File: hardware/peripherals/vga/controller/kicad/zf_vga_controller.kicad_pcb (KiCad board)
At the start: 2 copper layers, 98 x 40 mm, 17 parts, among them J1 Conn_01x09, Q1 BC547, SW1 SW_Push_Dual, SW2 SW_Push_Dual, SW3 SW_Push_Dual, SW4 SW_Push_Dual, SW5 SW_Push_Dual, SW6 SW_Push_Dual, U1 74HC541

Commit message: Final controller and Gerber files
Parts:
- removed the Mount1 at (234.0, 71.0)
- removed the Mount1 at (234.0, 39.0)
- added Mount1: MountingHole_3.2mm_M3_Pad, MountingHole:MountingHole_3.2mm_M3_Pad, F.Cu at (236.0, 71.0)
- added Mount1: MountingHole_3.2mm_M3_Pad, MountingHole:MountingHole_3.2mm_M3_Pad, F.Cu at (236.0, 39.0)
- moved R1 14.3 mm to (225.0, 38.8)
- moved R2 12.0 mm to (225.0, 42.5), turned to 180 degrees
- moved SW6 11.1 mm to (229.7, 55.0), turned to 45 degrees
- moved Q1 9.53 mm to (217.4, 46.4)
- moved SW5 9.40 mm to (220.0, 64.7), turned to 315 degrees
- moved SW1 0.05 mm to (160.0, 45.3)
- moved SW2 0.05 mm to (160.0, 64.7)
- moved SW3 0.05 mm to (150.3, 55.0)
- moved SW4 0.05 mm to (169.7, 55.0)
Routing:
- net Net-(RN1-Pad7): track 54.0 -> 34.1 mm
- net Net-(RN1-Pad6): track 15.6 -> 30.1 mm
- net Net-(SW5-Pad2): track 21.4 -> 33.3 mm
- net Net-(SW6-Pad2): track 22.7 -> 34.4 mm
- net Net-(Q1-Pad2): track 6.05 -> 13.3 mm
- net Net-(Q1-Pad1): track 40.8 -> 35.1 mm
- net Net-(J1-Pad9): track 11.5 -> 7.98 mm
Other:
- board size 98 x 40 mm -> 100 x 40 mm
- board text added: "Z-FIGHTER VGA Controller @tangent3D 2022"
- board text removed: "Z-FIGHTER VGA Module Controller @tangent3D 2022"

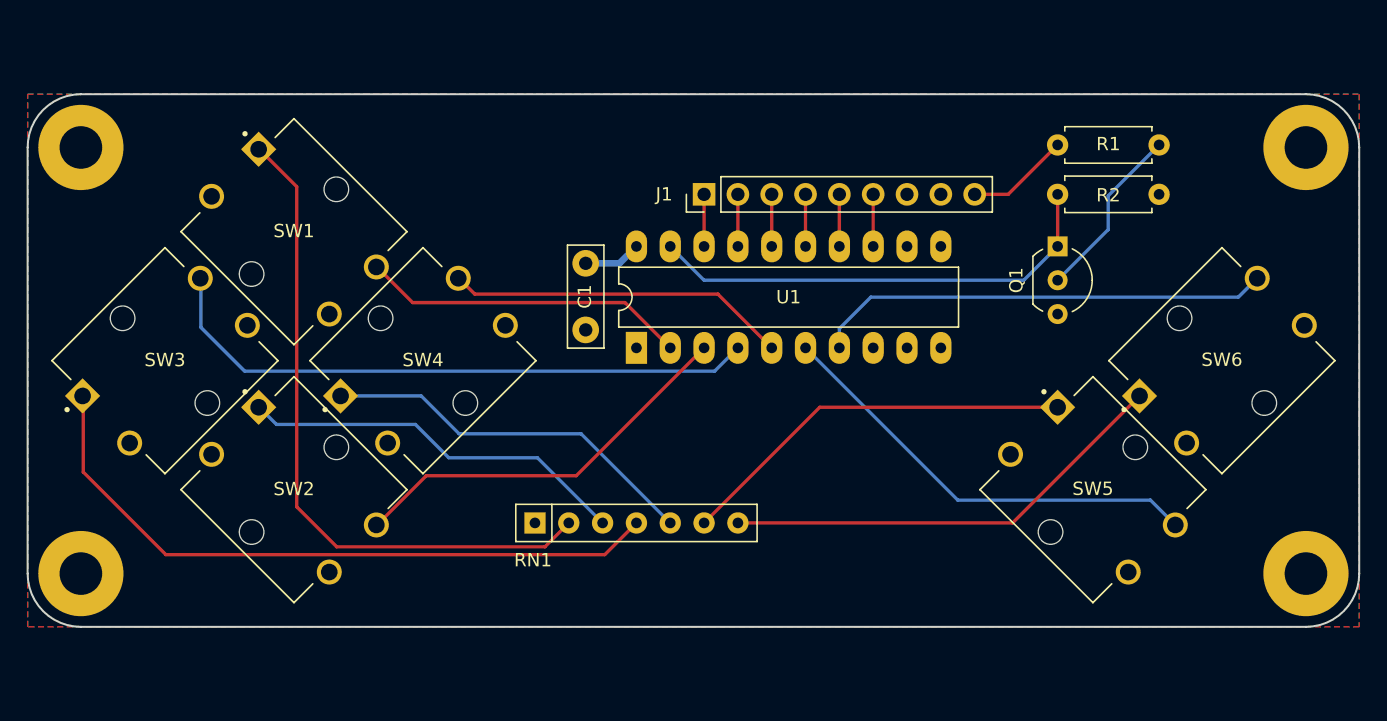
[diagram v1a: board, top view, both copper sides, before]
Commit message: Rounded corners
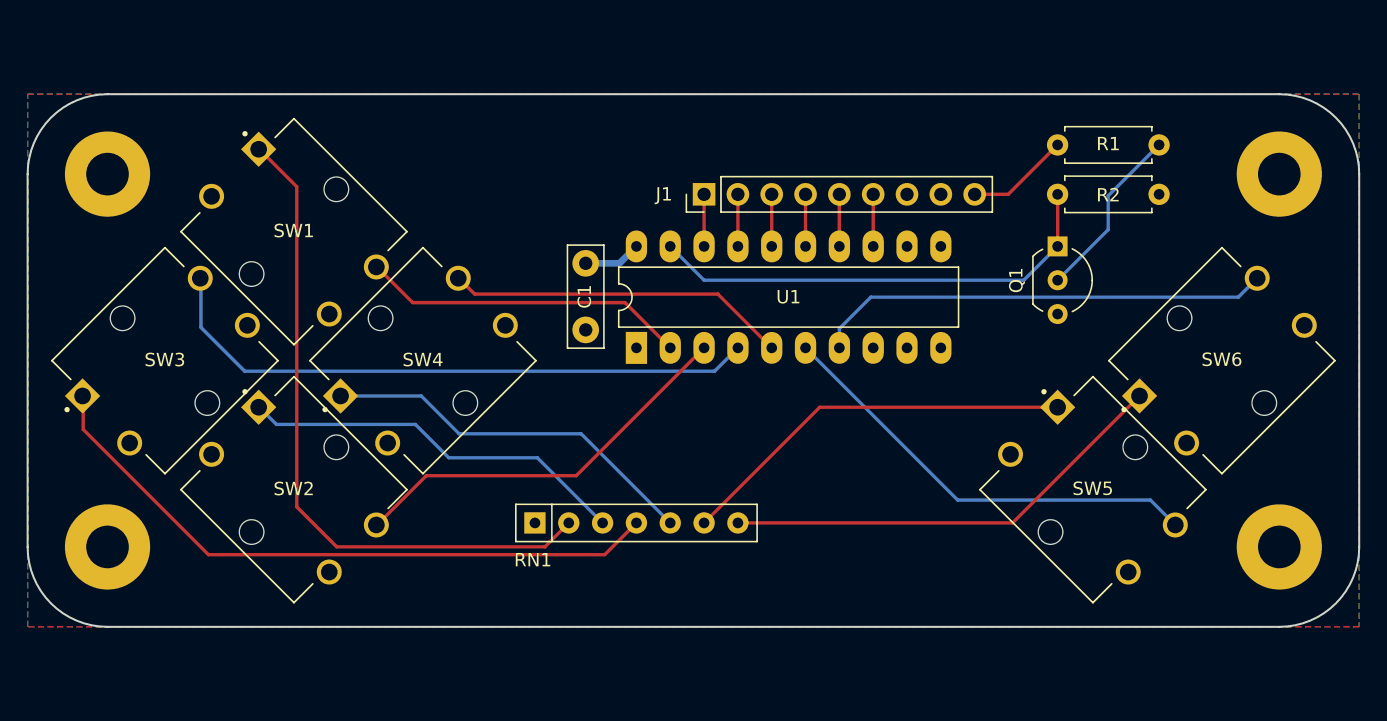
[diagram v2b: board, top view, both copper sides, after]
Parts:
- removed the Mount1 at (236.0, 71.0)
- removed the Mount1 at (236.0, 39.0)
- removed the Mount1 at (144.0, 71.0)
- removed the Mount1 at (144.0, 39.0)
- added Mount1: MountingHole_3.2mm_M3_Pad, MountingHole:MountingHole_3.2mm_M3_Pad, F.Cu at (234.0, 69.0)
- added Mount1: MountingHole_3.2mm_M3_Pad, MountingHole:MountingHole_3.2mm_M3_Pad, F.Cu at (234.0, 41.0)
- added Mount1: MountingHole_3.2mm_M3_Pad, MountingHole:MountingHole_3.2mm_M3_Pad, F.Cu at (146.0, 69.0)
- added Mount1: MountingHole_3.2mm_M3_Pad, MountingHole:MountingHole_3.2mm_M3_Pad, F.Cu at (146.0, 41.0)
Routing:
- net Net-(RN1-Pad4): track 50.8 -> 48.9 mm
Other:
- outline, holes or cut-outs redrawn

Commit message: Moved components to back of board
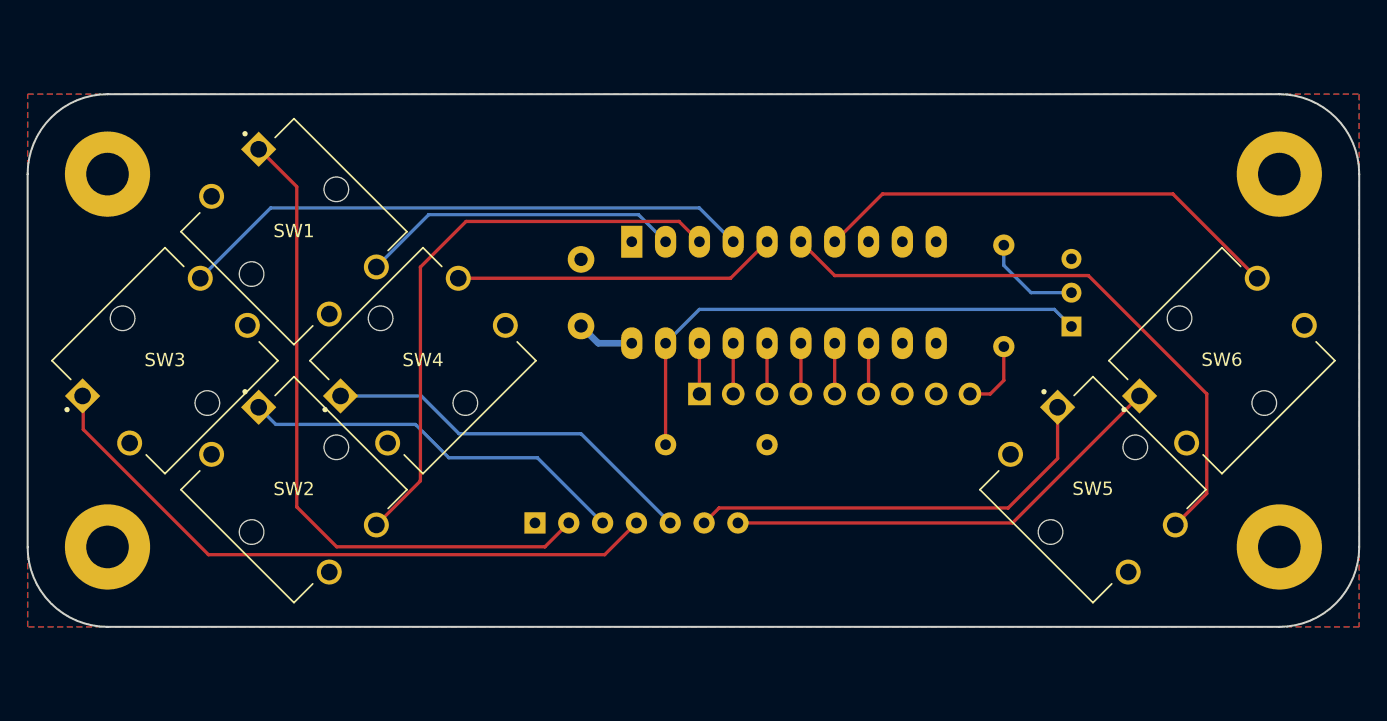
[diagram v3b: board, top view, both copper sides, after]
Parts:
- C1, J1, Q1, R1, R2, RN1, U1: moved to B.Cu
- moved R2 34.9 mm to (195.5, 61.3)
- moved J1 15.0 mm to (190.4, 57.5), turned to 270 degrees
- moved R1 13.9 mm to (213.3, 46.3), turned to 270 degrees
- moved U1 7.98 mm to (185.4, 46.1), turned to 270 degrees
- moved Q1 6.10 mm to (218.4, 52.4), turned to 90 degrees
- moved C1 4.72 mm to (181.6, 52.4), turned to 90 degrees
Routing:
- net Net-(SW2-Pad2): track 30.1 -> 43.7 mm
- net Net-(SW5-Pad2): track 33.3 -> 46.0 mm
- net Net-(Q1-Pad2): track 13.3 -> 7.45 mm
- net Net-(Q1-Pad1): track 35.1 -> 39.7 mm
- net Net-(SW3-Pad2): track 46.1 -> 43.3 mm
- net Net-(J1-Pad9): track 7.98 -> 5.50 mm
- net Net-(RN1-Pad6): track 30.1 -> 32.4 mm
- net Net-(SW6-Pad2): track 34.4 -> 35.8 mm
- net Net-(SW4-Pad2): track 25.7 -> 24.3 mm
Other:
- board text added: "Z-FIGHTER VGA Controller Rev. 1 @tangent3D 2022"
- board text removed: "Z-FIGHTER VGA Controller @tangent3D 2022"

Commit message: Redesigned controller around '241 buffer, added 2 extra buttons, increased height of PCB, added DE-9 connector
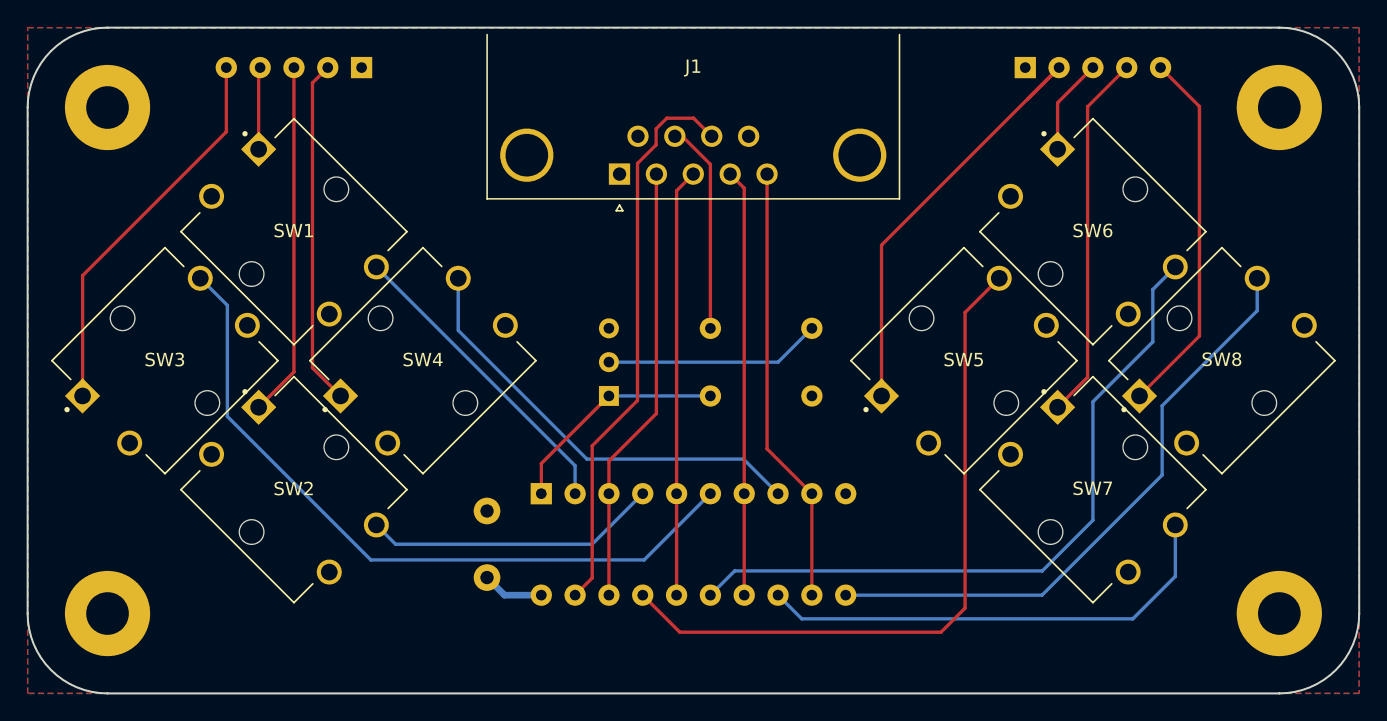
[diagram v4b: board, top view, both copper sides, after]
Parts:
- removed the Mount1 at (234.0, 69.0)
- removed the Mount1 at (234.0, 41.0)
- removed the Mount1 at (146.0, 69.0)
- removed the Mount1 at (146.0, 41.0)
- added Mount1: MountingHole_3.2mm_M3_Pad, MountingHole:MountingHole_3.2mm_M3_Pad, F.Cu at (234.0, 74.0)
- added Mount1: MountingHole_3.2mm_M3_Pad, MountingHole:MountingHole_3.2mm_M3_Pad, F.Cu at (234.0, 36.0)
- added Mount1: MountingHole_3.2mm_M3_Pad, MountingHole:MountingHole_3.2mm_M3_Pad, F.Cu at (146.0, 74.0)
- added Mount1: MountingHole_3.2mm_M3_Pad, MountingHole:MountingHole_3.2mm_M3_Pad, F.Cu at (146.0, 36.0)
- added RN2: R_Network04, Resistor_THT:R_Array_SIP5, B.Cu at (214.9, 33.0)
- added SW5: SW_Push_Dual, zf_vga_controller:SW_B3F-4050, F.Cu at (210.3, 55.0)
- added SW6: SW_Push_Dual, zf_vga_controller:SW_B3F-4050, F.Cu at (220.0, 45.3)
- J1: value Conn_01x09 -> DB9_Female; footprint Connector_PinHeader_2.54mm:PinHeader_1x09_P2.54mm_Vertical -> Connector_Dsub:DSUB-9_Female_Horizontal_P2.77x2.84mm_EdgePinOffset7.70mm_Housed_MountingHolesOffset9.12mm; moved to F.Cu
- RN1: value 10KΩ -> R_Network04; footprint Resistor_THT:R_Array_SIP7 -> Resistor_THT:R_Array_SIP5
- U1: value 74HC541 -> 74HC241; footprint Package_DIP:DIP-20_W7.62mm_LongPads -> Package_DIP:DIP-20_W7.62mm
- moved RN1 36.6 mm to (165.1, 33.0), turned to 180 degrees
- moved Q1 35.1 mm to (183.7, 57.7)
- moved C1 20.2 mm to (174.5, 71.3)
- moved U1 20.1 mm to (178.6, 65.0)
- moved J1 17.6 mm to (184.4, 41.0), turned to 180 degrees
- moved R1 15.7 mm to (198.9, 52.6), turned to 180 degrees
- moved R2 4.97 mm to (198.9, 57.7)
- renumbered SW5 to SW7, SW6 to SW8
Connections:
- net Net-(RN1-Pad3) renamed SW2
- net Net-(SW1-Pad2) renamed 1A1
- J1 pad 1: Net-(J1-Pad1) -> VCC
- J1 pad 2: Net-(J1-Pad2) -> PA0
- J1 pad 3: Net-(J1-Pad3) -> PA1
- J1 pad 4: Net-(J1-Pad4) -> PA2
- J1 pad 5: Net-(J1-Pad5) -> PA3
- J1 pad 6: Net-(J1-Pad6) -> GND
- J1 pad 7: VCC -> EN1
- J1 pad 8: GND -> EN2
- Q1 pad 1: Net-(Q1-Pad1) -> ~EN1
- R1 pad 2: Net-(J1-Pad9) -> EN1
- R2 pad 2: Net-(Q1-Pad1) -> ~EN1
- RN1 pad 2: Net-(RN1-Pad2) -> SW4
- RN1 pad 4: Net-(RN1-Pad4) -> SW1
- RN1 pad 5: Net-(RN1-Pad5) -> SW3
- SW1 pad 1: Net-(RN1-Pad2) -> SW1
- SW2 pad 2: Net-(SW2-Pad2) -> 1A2
- SW3 pad 1: Net-(RN1-Pad4) -> SW3
- SW3 pad 2: Net-(SW3-Pad2) -> 1A3
- SW4 pad 1: Net-(RN1-Pad5) -> SW4
- SW4 pad 2: Net-(SW4-Pad2) -> 1A4
- SW7 pad 1: Net-(RN1-Pad6) -> Net-(RN2-Pad4)
- SW7 pad 2: Net-(SW5-Pad2) -> 2A3
- SW8 pad 1: Net-(RN1-Pad7) -> Net-(RN2-Pad5)
- SW8 pad 2: Net-(SW6-Pad2) -> 2A4
- U1 pad 1: GND -> ~EN1
- U1 pad 11: Net-(U1-Pad11) -> 2A4
- U1 pad 12: Net-(U1-Pad12) -> PA3
- U1 pad 13: Net-(J1-Pad6) -> 2A3
- U1 pad 14: Net-(J1-Pad5) -> PA2
- U1 pad 15: Net-(J1-Pad4) -> 2A2
- U1 pad 16: Net-(J1-Pad3) -> PA1
- U1 pad 17: Net-(J1-Pad2) -> 2A1
- U1 pad 18: Net-(J1-Pad1) -> PA0
- U1 pad 19: Net-(Q1-Pad1) -> EN2
- U1 pad 3: Net-(SW2-Pad2) -> PA0
- U1 pad 4: Net-(SW3-Pad2) -> 1A2
- U1 pad 5: Net-(SW4-Pad2) -> PA1
- U1 pad 6: Net-(SW5-Pad2) -> 1A3
- U1 pad 7: Net-(SW6-Pad2) -> PA2
- U1 pad 8: GND -> 1A4
- U1 pad 9: GND -> PA3
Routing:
- net 1A3: track 0.00 -> 54.0 mm
- net 2A2: track 0.00 -> 52.6 mm
- net 2A1: track 0.00 -> 51.9 mm
- net Net-(RN1-Pad2): track 50.4 -> 0.00 mm
- net Net-(RN1-Pad4): track 48.9 -> 0.00 mm
- net Net-(SW5-Pad2): track 46.0 -> 0.00 mm
- net 2A4: track 0.00 -> 45.2 mm
- net Net-(SW2-Pad2): track 43.7 -> 0.00 mm
- net Net-(SW3-Pad2): track 43.3 -> 0.00 mm
- net EN2: track 0.00 -> 42.6 mm
- net Net-(Q1-Pad1): track 39.7 -> 0.00 mm
- net Net-(SW6-Pad2): track 35.8 -> 0.00 mm
- net 2A3: track 0.00 -> 35.8 mm
- net Net-(RN1-Pad7): track 34.1 -> 0.00 mm
- net Net-(RN2-Pad2): track 0.00 -> 33.6 mm
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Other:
- board size 100 x 40 mm -> 100 x 50 mm
- board text added: "Z-FIGHTER VGA Controller Rev. 2 @tangent3D 2022"
- board text removed: "Z-FIGHTER VGA Controller Rev. 1 @tangent3D 2022"

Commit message: Routing
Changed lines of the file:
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@@
   (segment (start 210.4 51.388907) (end 212.966043 48.822864) (width 0.25) (layer F.Cu) (net 22))
   (segment (start 210.4 73.6) (end 210.4 51.388907) (width 0.25) (layer F.Cu) (net 22))
+  (segment (start 224.5 49.663276) (end 226.188941 47.974335) (width 0.25) (layer B.Cu) (net 23))
+  (segment (start 224.5 53.6) (end 224.5 49.663276) (width 0.25) (layer B.Cu) (net 23))
+  (segment (start 216.2 70.8) (end 221.4 65.6) (width 0.25) (layer B.Cu) (net 23))
+  (segment (start 221.4 56.7) (end 224.5 53.6) (width 0.25) (layer B.Cu) (net 23))
+  (segment (start 193.095 70.8) (end 216.2 70.8) (width 0.25) (layer B.Cu) (net 23))
+  (segment (start 221.4 65.6) (end 221.4 56.7) (width 0.25) (layer B.Cu) (net 23))
   (segment (start 191.275 72.62) (end 193.095 70.8) (width 0.25) (layer B.Cu) (net 23))
-  (segment (start 193.095 70.8) (end 216.2 70.8) (width 0.25) (layer B.Cu) (net 23))
-  (segment (start 216.2 70.8) (end 220 67) (width 0.25) (layer B.Cu) (net 23))
-  (segment (start 220 67) (end 220 58.1) (width 0.25) (layer B.Cu) (net 23))
-  (segment (start 220 58.1) (end 224.5 53.6) (width 0.25) (layer B.Cu) (net 23))
-  (segment (start 224.5 53.6) (end 224.5 49.663276) (width 0.25) (layer B.Cu) (net 23))
-  (segment (start 224.5 49.663276) (end 226.188941 47.974335) (width 0.25) (layer B.Cu) (net 23))
   (segment (start 226.188941 71.211059) (end 226.188941 67.349061) (width 0.25) (layer B.Cu) (net 25))
   (segment (start 223 74.4) (end 226.188941 71.211059) (width 0.25) (layer B.Cu) (net 25))

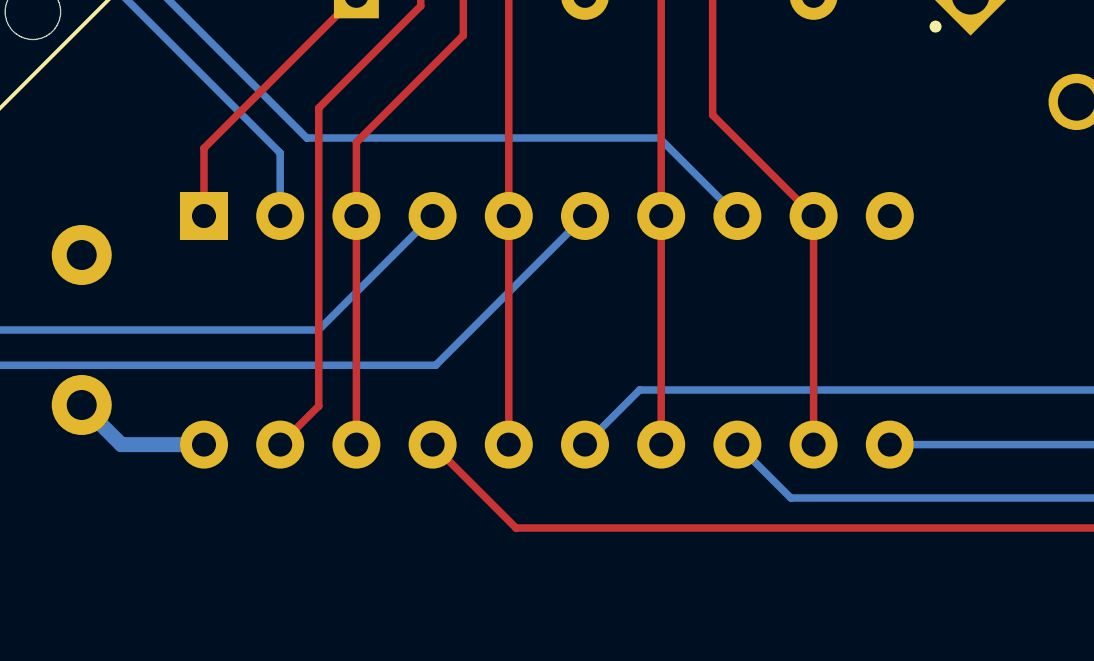
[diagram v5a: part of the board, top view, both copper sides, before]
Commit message: U1 footprint to LongPads
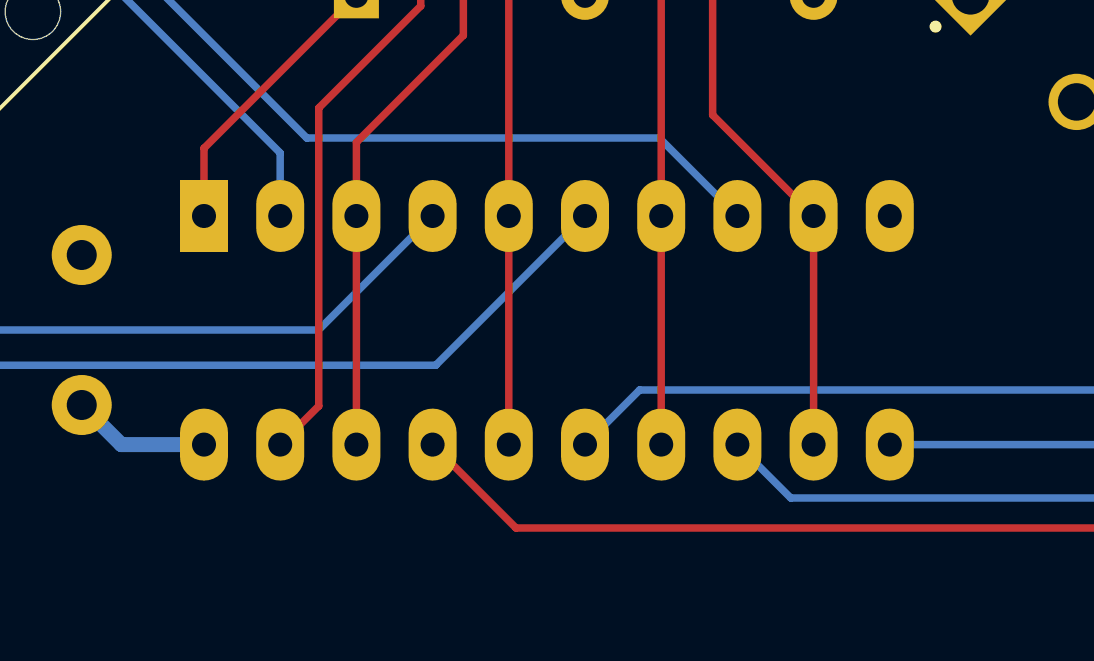
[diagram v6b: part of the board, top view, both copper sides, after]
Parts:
- U1: footprint Package_DIP:DIP-20_W7.62mm -> Package_DIP:DIP-20_W7.62mm_LongPads
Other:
- board text added: "Z-FIGHTER VGA Controller Rev. 2a @tangent3D 2022"
- board text removed: "Z-FIGHTER VGA Controller Rev. 2 @tangent3D 2022"
